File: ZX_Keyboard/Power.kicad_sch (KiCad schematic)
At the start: 0 parts

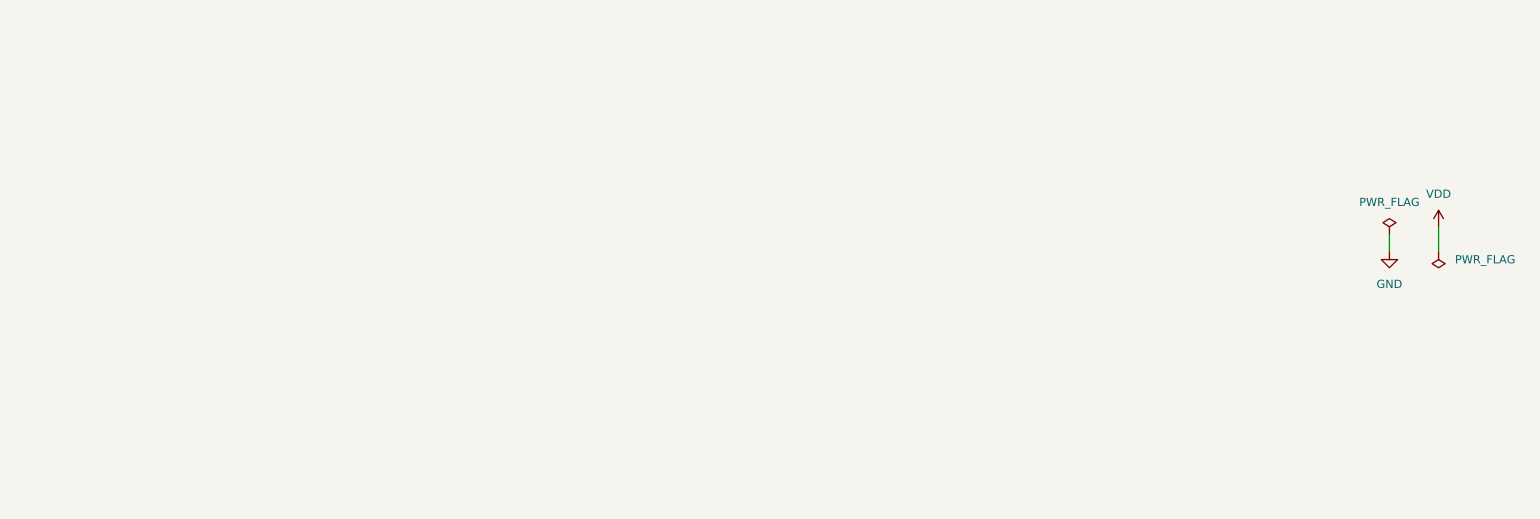
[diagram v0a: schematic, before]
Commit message: add connector sheet
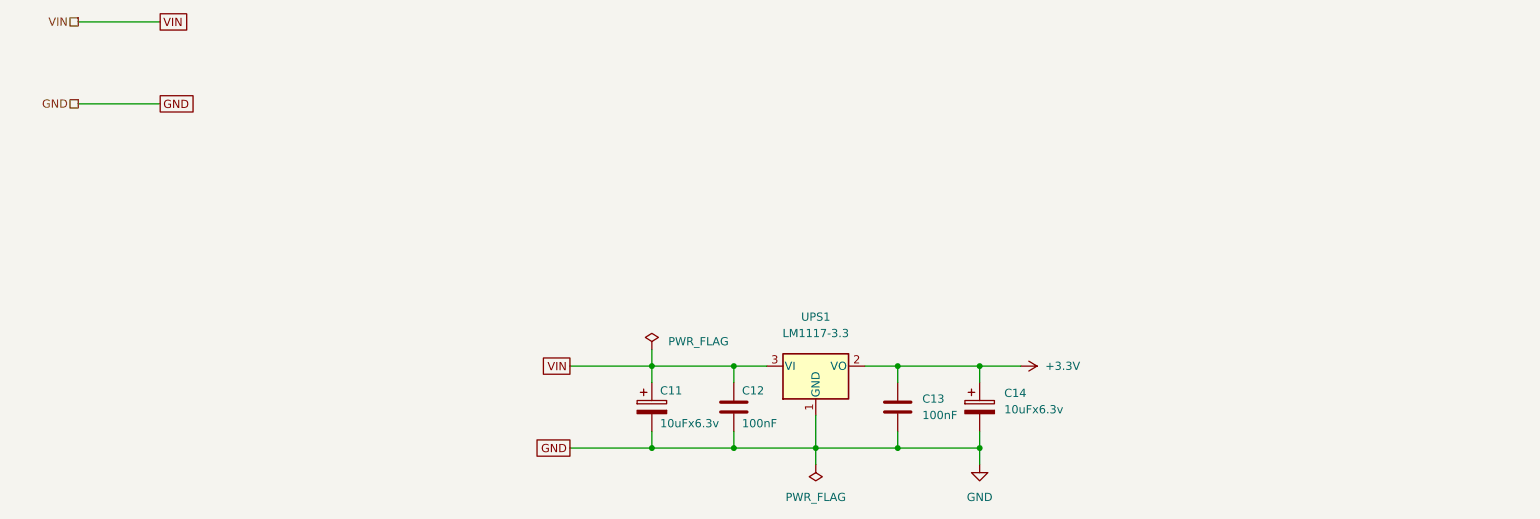
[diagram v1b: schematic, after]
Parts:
- added C11, C14: 10uFx6.3v, Capacitor_Tantalum_SMD:CP_EIA-3528-12_Kemet-T_Pad1.50x2.35mm_HandSolder, symbol Device:C_Polarized
- added C12, C13: 100nF, Capacitor_SMD:C_0805_2012Metric_Pad1.18x1.45mm_HandSolder, symbol Device:C
- added UPS1: LM1117-3.3, Package_TO_SOT_SMD:SOT-223-3_TabPin2, symbol Regulator_Linear:LM1117-3.3
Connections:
- net GND: now also C11.2, C12.2, C13.2, C14.2, UPS1.1 (GND)
- new net +3.3V: C13.1, C14.1, UPS1.2 (VO)
- new net VIN: C11.1, C12.1, UPS1.3 (VI)
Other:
- title: (none) -> USB_Keyboard for ZX-Spectrum

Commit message: improve zx_keyboard schematic
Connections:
- net VIN renamed VCC
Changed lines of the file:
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@@
+    (stroke (width 0) (type default) (color 0 0 0 0))
+  )
+  (wire (pts (xy 139.7 88.9) (xy 139.7 91.44))
     (stroke (width 0) (type default) (color 0 0 0 0))
   )
@@
     )
     (property "Value" "PWR_FLAG" (id 1) (at 129.54 87.6299 0)
-      (effects (font (size 1.27 1.27)) (justify left))
+      (effects (font (size 1.27 1.27)) (justify left) hide)
     )
     (property "Footprint" "" (id 2) (at 127 88.9 0)
@@
   (symbol (lib_id "power:+3.3V") (at 184.15 91.44 270) (unit 1)
     (in_bom yes) (on_board yes) (fields_autoplaced)
-    (property "Reference" "#PWR024" (id 0) (at 180.34 91.44 0)
+    (property "Reference" "#PWR025" (id 0) (at 180.34 91.44 0)
       (effects (font (size 1.27 1.27)) hide)
     )
@@
     (pin "2")
   )
+  (symbol (lib_id "power:VCC") (at 139.7 88.9 0) (unit 1)
+    (in_bom yes) (on_board yes) (fields_autoplaced)
+    (property "Reference" "#PWR024" (id 0) (at 139.7 92.71 0)
+      (effects (font (size 1.27 1.27)) hide)
+    )
+    (property "Value" "VCC" (id 1) (at 139.7 83.82 0))
+    (property "Footprint" "" (id 2) (at 139.7 88.9 0)
+      (effects (font (size 1.27 1.27)) hide)
+    )
+    (property "Datasheet" "" (id 3) (at 139.7 88.9 0)
+      (effects (font (size 1.27 1.27)) hide)
+    )
+    (pin "1")
+  )
   (symbol (lib_id "power:GND") (at 177.8 106.68 0) (unit 1)
     (in_bom yes) (on_board yes) (fields_autoplaced)
-    (property "Reference" "#PWR025" (id 0) (at 177.8 113.03 0)
-      (effects (font (size 1.27 1.27)) hide)
-    )
+    (property "Reference" "#PWR026" (id 0) (at 177.8 113.03 0)
+      (effects (font (size 1.27 1.27)) hide)
+    )

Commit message: update and fix schematic
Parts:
- added L1: 100uH, CD inductor:CD43, symbol Device:L
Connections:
- net VCC: now also L1.2
- new net VIN+5V: L1.1
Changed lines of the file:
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@@
     (stroke (width 0) (type default) (color 0 0 0 0))
   )
-  (wire (pts (xy 114.3 104.14) (xy 127 104.14))
+  (wire (pts (xy 88.9 104.14) (xy 127 104.14))
     (stroke (width 0) (type default) (color 0 0 0 0))
   )
@@
     (stroke (width 0) (type default) (color 0 0 0 0))
   )
-  (wire (pts (xy 114.3 91.44) (xy 127 91.44))
+  (wire (pts (xy 115.57 91.44) (xy 127 91.44))
     (stroke (width 0) (type default) (color 0 0 0 0))
   )
@@
     (stroke (width 0) (type default) (color 0 0 0 0))
   )
+  (wire (pts (xy 88.9 91.44) (xy 107.95 91.44))
+    (stroke (width 0) (type default) (color 0 0 0 0))
+  )
   (wire (pts (xy 165.1 104.14) (xy 177.8 104.14))
     (stroke (width 0) (type default) (color 0 0 0 0))
@@
     )
   )
-  (global_label "VIN" (shape passive) (at 114.3 91.44 180) (fields_autoplaced)
+  (global_label "VIN+5V" (shape passive) (at 88.9 91.44 180) (fields_autoplaced)
     (effects (font (size 1.27 1.27)) (justify right))
-    (property "Intersheet References" "${INTERSHEET_REFS}" (id 0) (at 108.8631 91.3606 0)
+    (property "Intersheet References" "${INTERSHEET_REFS}" (id 0) (at 79.5926 91.3606 0)
       (effects (font (size 1.27 1.27)) (justify right) hide)
     )
   )
-  (global_label "GND" (shape passive) (at 114.3 104.14 180) (fields_autoplaced)
+  (global_label "GND" (shape passive) (at 88.9 104.14 180) (fields_autoplaced)
     (effects (font (size 1.27 1.27)) (justify right))
-    (property "Intersheet References" "${INTERSHEET_REFS}" (id 0) (at 108.0164 104.0606 0)
+    (property "Intersheet References" "${INTERSHEET_REFS}" (id 0) (at 82.6164 104.0606 0)
       (effects (font (size 1.27 1.27)) (justify right) hide)
     )
   )
-  (global_label "VIN" (shape passive) (at 50.8 38.1 0) (fields_autoplaced)
+  (global_label "VIN+5V" (shape passive) (at 50.8 38.1 0) (fields_autoplaced)
     (effects (font (size 1.27 1.27)) (justify left))
-    (property "Intersheet References" "${INTERSHEET_REFS}" (id 0) (at 56.2369 38.0206 0)
+    (property "Intersheet References" "${INTERSHEET_REFS}" (id 0) (at 60.1074 38.0206 0)
       (effects (font (size 1.27 1.27)) (justify left) hide)
     )
   )
-  (hierarchical_label "VIN" (shape passive) (at 38.1 38.1 180)
+  (hierarchical_label "VIN+5V" (shape passive) (at 38.1 38.1 180)
     (effects (font (size 1.27 1.27)) (justify right))
   )
@@
       (effects (font (size 1.27 1.27)) hide)
     )
+    (pin "1")
+    (pin "2")
+  )
+  (symbol (lib_id "Device:L") (at 111.76 91.44 90) (unit 1)
+    (in_bom yes) (on_board yes)
+    (property "Reference" "L1" (id 0) (at 111.76 88.9 90))
+    (property "Value" "100uH" (id 1) (at 111.76 92.71 90))
+    (property "Footprint" "CD inductor:CD43" (id 2) (at 111.76 91.44 0)
+      (effects (font (size 1.27 1.27)) hide)
+    )
+    (property "Datasheet" "~" (id 3) (at 111.76 91.44 0)
+      (effects (font (size 1.27 1.27)) hide)
+    )

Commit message: update schematic and pcb
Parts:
- C11, C14: footprint Capacitor_Tantalum_SMD:CP_EIA-3528-12_Kemet-T_Pad1.50x2.35mm_HandSolder -> Capacitor_Tantalum_SMD:CP_EIA-3216-18_Kemet-A_Pad1.58x1.35mm_HandSolder
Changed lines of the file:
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@@
       (effects (font (size 1.27 1.27)) (justify left))
     )
-    (property "Footprint" "Capacitor_Tantalum_SMD:CP_EIA-3528-12_Kemet-T_Pad1.50x2.35mm_HandSolder" (id 2) (at 127.9652 101.6 0)
+    (property "Footprint" "Capacitor_Tantalum_SMD:CP_EIA-3216-18_Kemet-A_Pad1.58x1.35mm_HandSolder" (id 2) (at 127.9652 101.6 0)
       (effects (font (size 1.27 1.27)) hide)
     )
@@
       (effects (font (size 1.27 1.27)) (justify left))
     )
-    (property "Footprint" "Capacitor_Tantalum_SMD:CP_EIA-3528-12_Kemet-T_Pad1.50x2.35mm_HandSolder" (id 2) (at 178.7652 101.6 0)
+    (property "Footprint" "Capacitor_Tantalum_SMD:CP_EIA-3216-18_Kemet-A_Pad1.58x1.35mm_HandSolder" (id 2) (at 178.7652 101.6 0)
       (effects (font (size 1.27 1.27)) hide)
     )

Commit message: update keyboard pcb
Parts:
- renumbered C11 to CPS1, C12 to CPS2, C13 to CPS3, C14 to CPS4, L1 to LPS1
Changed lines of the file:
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@@
   (symbol (lib_id "power:+3.3V") (at 184.15 91.44 270) (unit 1)
     (in_bom yes) (on_board yes) (fields_autoplaced)
-    (property "Reference" "#PWR025" (id 0) (at 180.34 91.44 0)
+    (property "Reference" "#PWR027" (id 0) (at 180.34 91.44 0)
       (effects (font (size 1.27 1.27)) hide)
     )
@@
   (symbol (lib_id "Device:C_Polarized") (at 127 97.79 0) (unit 1)
     (in_bom yes) (on_board yes)
-    (property "Reference" "C11" (id 0) (at 128.27 95.25 0)
+    (property "Reference" "CPS1" (id 0) (at 128.27 95.25 0)
       (effects (font (size 1.27 1.27)) (justify left))
     )
@@
   (symbol (lib_id "Device:L") (at 111.76 91.44 90) (unit 1)
     (in_bom yes) (on_board yes)
-    (property "Reference" "L1" (id 0) (at 111.76 88.9 90))
+    (property "Reference" "LPS1" (id 0) (at 111.76 88.9 90))
     (property "Value" "100uH" (id 1) (at 111.76 92.71 90))
     (property "Footprint" "CD inductor:CD43" (id 2) (at 111.76 91.44 0)
@@
   (symbol (lib_id "Device:C_Polarized") (at 177.8 97.79 0) (unit 1)
     (in_bom yes) (on_board yes) (fields_autoplaced)
-    (property "Reference" "C14" (id 0) (at 181.61 95.6309 0)
+    (property "Reference" "CPS4" (id 0) (at 181.61 95.6309 0)
       (effects (font (size 1.27 1.27)) (justify left))
     )
@@
   (symbol (lib_id "Device:C") (at 165.1 97.79 0) (unit 1)
     (in_bom yes) (on_board yes) (fields_autoplaced)
-    (property "Reference" "C13" (id 0) (at 168.91 96.5199 0)
+    (property "Reference" "CPS3" (id 0) (at 168.91 96.5199 0)
       (effects (font (size 1.27 1.27)) (justify left))
     )
@@
   (symbol (lib_id "Device:C") (at 139.7 97.79 0) (unit 1)
     (in_bom yes) (on_board yes)
-    (property "Reference" "C12" (id 0) (at 140.97 95.25 0)
+    (property "Reference" "CPS2" (id 0) (at 140.97 95.25 0)
       (effects (font (size 1.27 1.27)) (justify left))
     )
@@
   (symbol (lib_id "power:VCC") (at 139.7 88.9 0) (unit 1)
     (in_bom yes) (on_board yes) (fields_autoplaced)
-    (property "Reference" "#PWR024" (id 0) (at 139.7 92.71 0)
+    (property "Reference" "#PWR026" (id 0) (at 139.7 92.71 0)
       (effects (font (size 1.27 1.27)) hide)
     )
@@
   (symbol (lib_id "power:GND") (at 177.8 106.68 0) (unit 1)
     (in_bom yes) (on_board yes) (fields_autoplaced)
-    (property "Reference" "#PWR026" (id 0) (at 177.8 113.03 0)
+    (property "Reference" "#PWR028" (id 0) (at 177.8 113.03 0)
       (effects (font (size 1.27 1.27)) hide)
     )

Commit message: teracing and refactoring connectors
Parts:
- added DPS1: 1N5817, Diode_SMD:D_MiniMELF, symbol Device:D
- added JPS1: POWER, Connector_PinHeader_2.54mm:PinHeader_1x02_P2.54mm_Vertical, symbol Connector_Generic:Conn_01x02
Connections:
- net GND: now also JPS1.2 (Pin_2)
- net VIN+5V: now also DPS1.2 (A), JPS1.1 (Pin_1); no longer LPS1.1
- new net: DPS1.1 (K), LPS1.1
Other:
- moved on the sheet: CPS1, CPS2, CPS3, CPS4, LPS1, UPS1
